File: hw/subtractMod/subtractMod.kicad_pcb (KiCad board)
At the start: 2 copper layers, 53.8 x 42.4 mm, 39 parts, among them IC1 LMP2011, IC2 BUF04701, J1 Screw_Terminal_01x04, J2 Screw_Terminal_01x04, J3 Screw_Terminal_01x02, U1 TLV6001DCK, U2 AD8276, U3 AD8276, U4 AD8276

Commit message: changed tracks width
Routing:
- net -5V: track 62.2 -> 67.0 mm
- net Net-(IC1-Pad4): track 7.68 -> 3.23 mm, vias 1 -> 0
- net /offset_control/chan1_in: track 9.89 -> 5.94 mm
- net Net-(IC1-Pad1): track 15.2 -> 19.0 mm
- net Net-(C3-Pad1): track 5.59 -> 6.55 mm
- net Net-(RV3-Pad2): track 7.79 -> 6.93 mm
- net Net-(J1-Pad3): track 12.2 -> 11.7 mm

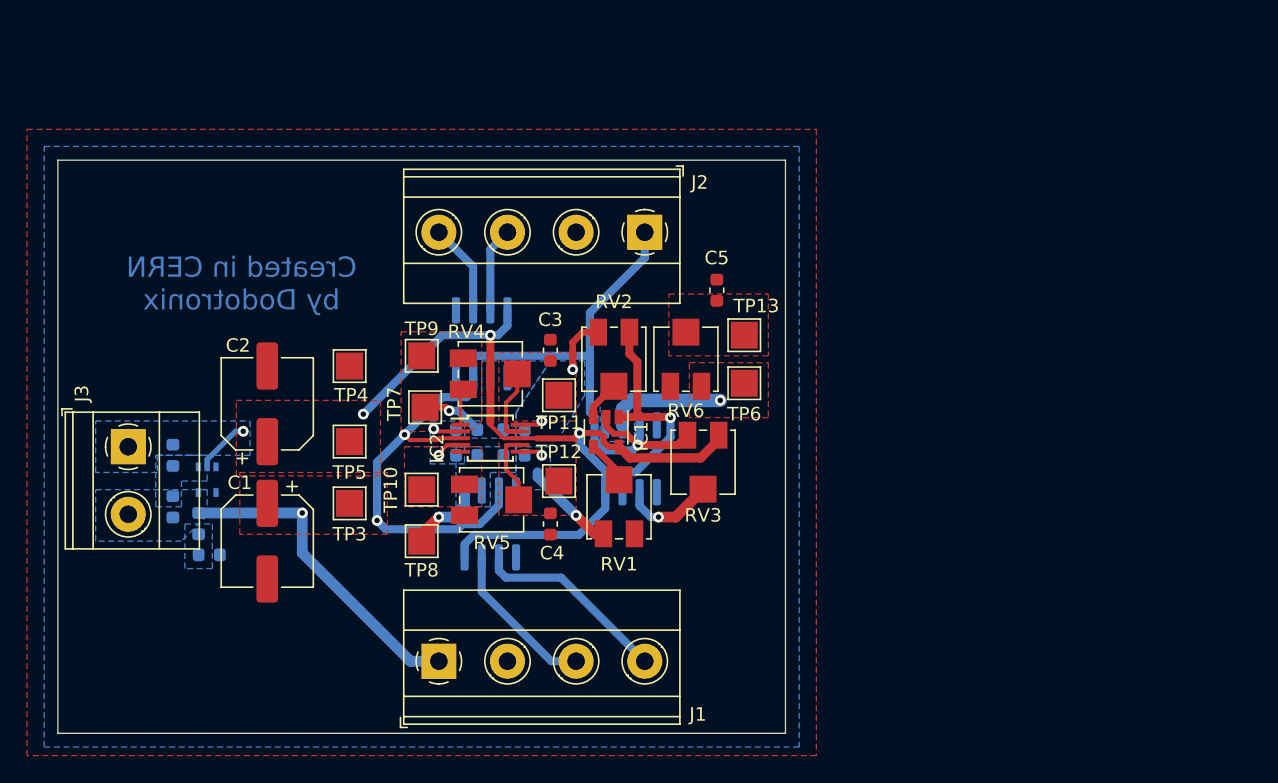
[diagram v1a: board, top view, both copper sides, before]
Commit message: updated schematics of subtraction module
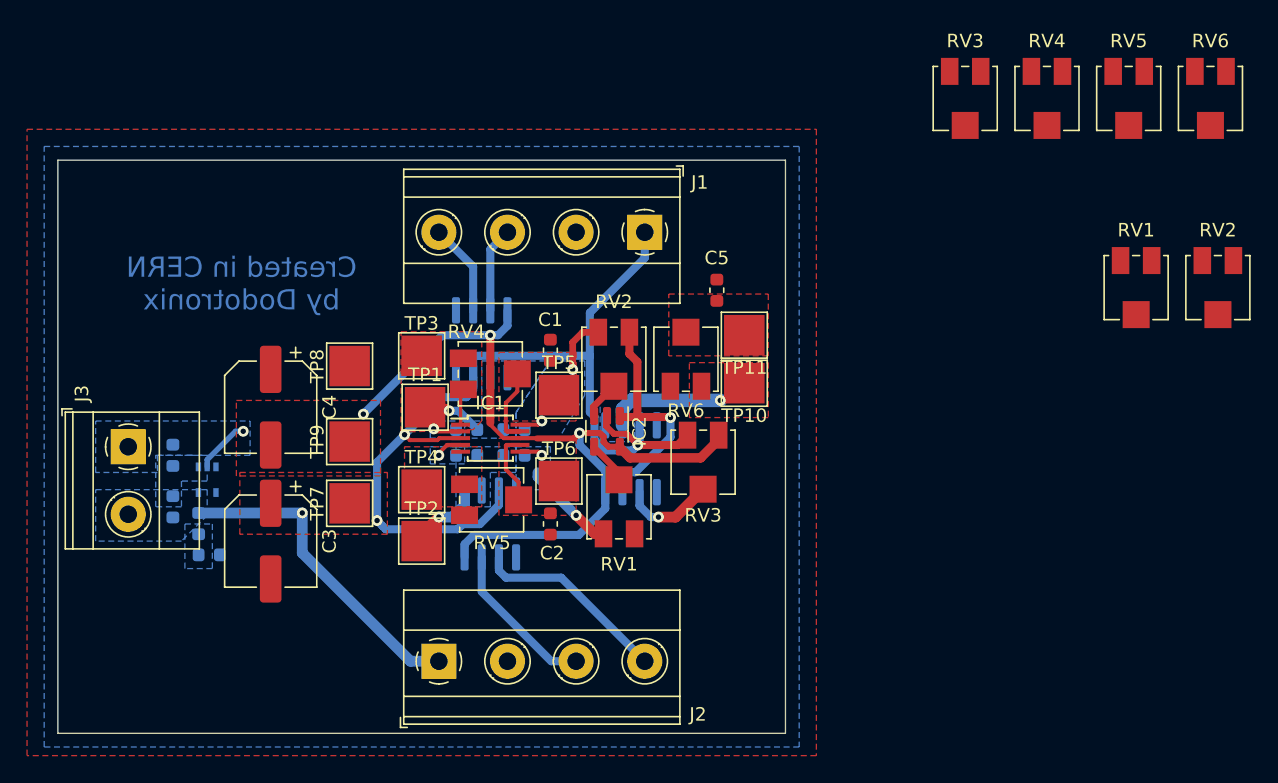
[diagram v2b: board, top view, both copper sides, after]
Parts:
- removed the C1 at (137.2, 105.4)
- removed the C2 at (137.2, 95.2)
- added C3: 47u, Capacitor_SMD:CP_Elec_6.3x5.9, F.Cu at (137.4, 105.4)
- added C4: 47u, Capacitor_SMD:CP_Elec_6.3x5.9, F.Cu at (137.4, 95.5)
- added RV1: R_Potentiometer_Trim, Potentiometer_SMD:Potentiometer_Bourns_3314J_Vertical, F.Cu at (201.5, 86.6)
- added RV2: R_Potentiometer_Trim, Potentiometer_SMD:Potentiometer_Bourns_3314J_Vertical, F.Cu at (207.5, 86.6)
- added RV3: R_Potentiometer_Trim, Potentiometer_SMD:Potentiometer_Bourns_3314J_Vertical, F.Cu at (188.8, 72.6)
- added RV4: R_Potentiometer_Trim, Potentiometer_SMD:Potentiometer_Bourns_3314J_Vertical, F.Cu at (194.9, 72.6)
- added RV5: R_Potentiometer_Trim, Potentiometer_SMD:Potentiometer_Bourns_3314J_Vertical, F.Cu at (200.9, 72.6)
- added RV6: R_Potentiometer_Trim, Potentiometer_SMD:Potentiometer_Bourns_3314J_Vertical, F.Cu at (207.0, 72.6)
- IC1: value LMP2011 -> AD8244; footprint Package_TO_SOT_SMD:SOT-23-5 -> Package_SO:MSOP-10_3x3mm_P0.5mm
- IC2: value BUF04701 -> LMP2011; footprint Package_SO:MSOP-10_3x3mm_P0.5mm -> Package_TO_SOT_SMD:SOT-23-5
- TP1: renamed from TP7; footprint TestPoint:TestPoint_Pad_2.0x2.0mm -> TestPoint:TestPoint_Pad_3.0x3.0mm
- TP10: renamed from TP6; footprint TestPoint:TestPoint_Pad_2.0x2.0mm -> TestPoint:TestPoint_Pad_3.0x3.0mm
- TP11: renamed from TP13; footprint TestPoint:TestPoint_Pad_2.0x2.0mm -> TestPoint:TestPoint_Pad_3.0x3.0mm
- TP2: renamed from TP8; footprint TestPoint:TestPoint_Pad_2.0x2.0mm -> TestPoint:TestPoint_Pad_3.0x3.0mm
- TP3: renamed from TP9; footprint TestPoint:TestPoint_Pad_2.0x2.0mm -> TestPoint:TestPoint_Pad_3.0x3.0mm
- TP4: renamed from TP10; footprint TestPoint:TestPoint_Pad_2.0x2.0mm -> TestPoint:TestPoint_Pad_3.0x3.0mm
- TP5: renamed from TP11; footprint TestPoint:TestPoint_Pad_2.0x2.0mm -> TestPoint:TestPoint_Pad_3.0x3.0mm
- TP6: renamed from TP12; footprint TestPoint:TestPoint_Pad_2.0x2.0mm -> TestPoint:TestPoint_Pad_3.0x3.0mm
- TP7: renamed from TP3; footprint TestPoint:TestPoint_Pad_2.0x2.0mm -> TestPoint:TestPoint_Pad_3.0x3.0mm
- TP8: renamed from TP4; footprint TestPoint:TestPoint_Pad_2.0x2.0mm -> TestPoint:TestPoint_Pad_3.0x3.0mm
- TP9: renamed from TP5; footprint TestPoint:TestPoint_Pad_2.0x2.0mm -> TestPoint:TestPoint_Pad_3.0x3.0mm
- moved IC2 8.65 mm to (162.3, 97.3), turned to -90 degrees
- moved IC1 8.58 mm to (153.7, 97.8), turned to 0 degrees
- renumbered C3 to C1, C4 to C2, J2 to J1, J1 to J2, R6 to R1, R7 to R2, R8 to R3, R9 to R4, R1 to R6, R2 to R7, U3 to U1, U4 to U2, U1 to U3, U2 to U4
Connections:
- C1 pad 1: Net-(C3-Pad1) -> Net-(IC1B-InB)
- C2 pad 1: Net-(C4-Pad1) -> Net-(IC1D-InD)
- IC1 pad 1: Net-(IC1-Pad1) -> Net-(IC1A-InA)
- IC1 pad 2: +5V -> Net-(IC1A-OutA)
- IC1 pad 3: Net-(IC1-Pad3) -> +5V
- IC1 pad 4: Net-(IC1-Pad4) -> /Input_channel/chan1_out
- IC1 pad 5: -5V -> Net-(IC1B-InB)
- IC2 pad 1: Net-(IC2-Pad1) -> Net-(IC2A-Vout)
- IC2 pad 2: Net-(IC2-Pad2) -> -5V
- IC2 pad 3: +5V -> Net-(IC2A-V+)
- IC2 pad 4: Net-(IC2-Pad4) -> Net-(IC2A-V-)
- IC2 pad 5: Net-(IC2-Pad5) -> +5V
- R1 pad 1: Net-(IC2-Pad2) -> Net-(IC1A-InA)
- R2 pad 1: Net-(IC2-Pad4) -> Net-(IC1C-InC)
- R3 pad 1: /offset_control/chan1_in -> /Input_channel/chan1_out
- R4 pad 1: /offset_control/chan2_in -> /Input_channel/chan2_out
- TP10 pad 1: Net-(RV6-Pad3) -> Net-(U4-SENSE)
- TP3 pad 1: Net-(IC2-Pad1) -> Net-(IC1A-OutA)
- TP4 pad 1: Net-(IC2-Pad5) -> Net-(IC1C-OutC)
- TP5 pad 1: Net-(C3-Pad1) -> Net-(IC1B-InB)
- TP6 pad 1: Net-(C4-Pad1) -> Net-(IC1D-InD)
- U1 pad 8: (no net) -> unconnected-(U1-Pad8)
- U2 pad 8: (no net) -> unconnected-(U2-Pad8)
- U4 pad 2: Net-(RV3-Pad2) -> Net-(U4--)
- U4 pad 3: Net-(IC1-Pad1) -> Net-(IC2A-Vout)
- U4 pad 5: Net-(RV6-Pad3) -> Net-(U4-SENSE)
- U4 pad 6: Net-(RV6-Pad3) -> Net-(U4-SENSE)
- U4 pad 8: (no net) -> unconnected-(U4-Pad8)
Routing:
- net Net-(U4-SENSE): track 0.00 -> 8.71 mm, vias 0 -> 1
- net Net-(RV6-Pad3): track 8.71 -> 0.00 mm, vias 1 -> 0
- net /Input_channel/sensA_out: track 4.54 -> 6.61 mm, vias 1 -> 2
- net Net-(IC2-Pad2): track 2.07 -> 0.00 mm, vias 1 -> 0
- net Net-(IC2-Pad4): track 2.02 -> 0.00 mm, vias 1 -> 0
- net /Input_channel/chan1_out: track 0.00 -> 2.02 mm, vias 0 -> 1
- net Net-(IC1D-InD): track 0.00 -> 1.72 mm, vias 0 -> 1
- net /offset_control/chan1_in: track 5.94 -> 4.22 mm, vias 2 -> 1
- net Net-(IC1C-InC): track 0.00 -> 1.72 mm, vias 0 -> 1
- net /offset_control/chan2_in: track 8.67 -> 6.94 mm, vias 2 -> 1
- added copper zone on B.Cu, net /Input_channel/chan1_out
- added copper zone on B.Cu, net /Input_channel/chan2_out
- added copper zone on B.Cu, net Net-(IC1A-InA)
- added copper zone on F.Cu, net Net-(IC1A-OutA)
- added copper zone on F.Cu, net Net-(IC1B-InB)
- added copper zone on B.Cu, net Net-(IC1C-InC)
- added copper zone on F.Cu, net Net-(IC1C-OutC)
- added copper zone on F.Cu, net Net-(IC1D-InD)
- added copper zone on B.Cu, net Net-(U4-SENSE)
- added copper zone on F.Cu, net Net-(U4-SENSE)
- removed copper zone on B.Cu, net /offset_control/chan1_in
- removed copper zone on B.Cu, net /offset_control/chan2_in
- removed copper zone on F.Cu, net Net-(C3-Pad1)
- removed copper zone on F.Cu, net Net-(C4-Pad1)
- removed copper zone on F.Cu, net Net-(IC2-Pad1)
- removed copper zone on B.Cu, net Net-(IC2-Pad2)
- removed copper zone on B.Cu, net Net-(IC2-Pad4)
- removed copper zone on F.Cu, net Net-(IC2-Pad5)
- removed copper zone on B.Cu, net Net-(RV6-Pad3)
- removed copper zone on F.Cu, net Net-(RV6-Pad3)
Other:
- net class Default removed
